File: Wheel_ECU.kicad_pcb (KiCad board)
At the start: 2 copper layers, 61 x 61 mm, 58 parts, among them J1 Conn_01x04, J2 Conn_01x04, J3 Conn_01x02, J4 Debug, U1 IFX9201SG, U2 TLE4964, U3 XMC1404_F064, U4 TLE7251

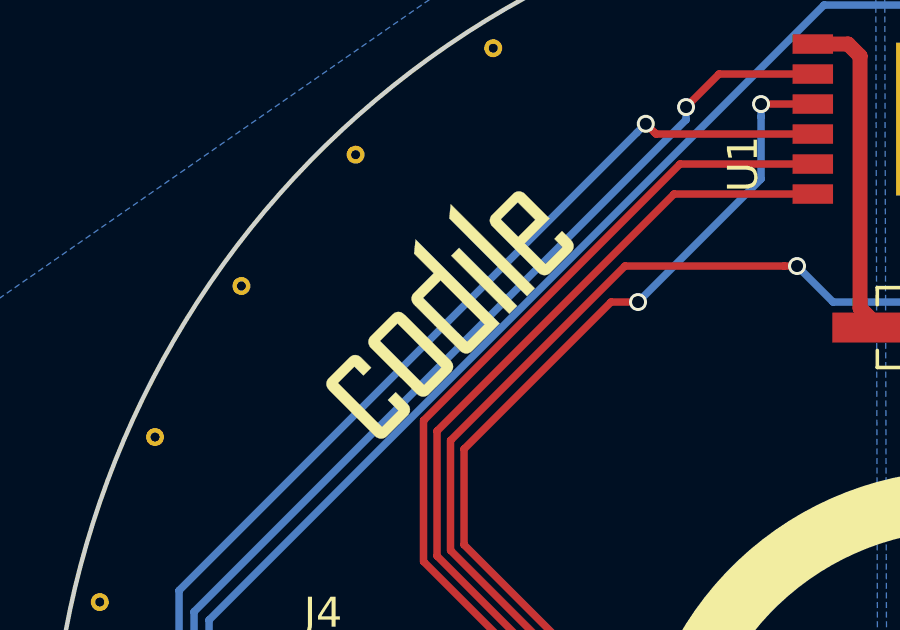
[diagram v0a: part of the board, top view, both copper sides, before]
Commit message: Remove the Codile logotype from the PCB
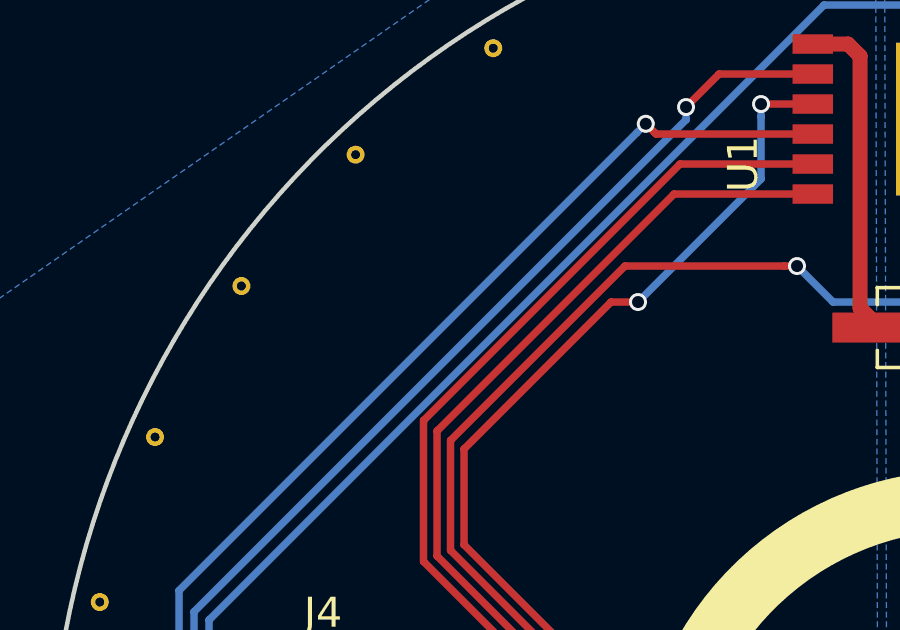
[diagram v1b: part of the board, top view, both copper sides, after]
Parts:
- removed the G*** at (114.2, 81.8)

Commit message: Move logotype
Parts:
- moved G*** 46.4 mm to (113.0, 81.3)
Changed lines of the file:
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@@
   )
   (module WheelECU:Logo_Wolley_Interconnect_SolderMask (layer F.Cu)
-    (at 156 98.9)
+    (at 113.03 81.28)
     (fp_text reference G*** (at 0 0) (layer F.SilkS) hide
       (effects (font (size 1.524 1.524) (thickness 0.3)))
